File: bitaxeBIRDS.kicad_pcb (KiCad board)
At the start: 6 copper layers, 65 x 120 mm, 204 parts, among them J1 XT30, J4 Conn_01x04, U12 TLV75512PDQNR, U13 EMC2103-2, U14 TLV75512PDQNR, U15 TLV75512PDQNR, U2 TPS546D24ARVFR, U3 TLV75512PDQNR, U5 TPS22919DCKR, U8 SN74AVC4T774, U9 Raspberry Pi Pico, Y2 50MHz

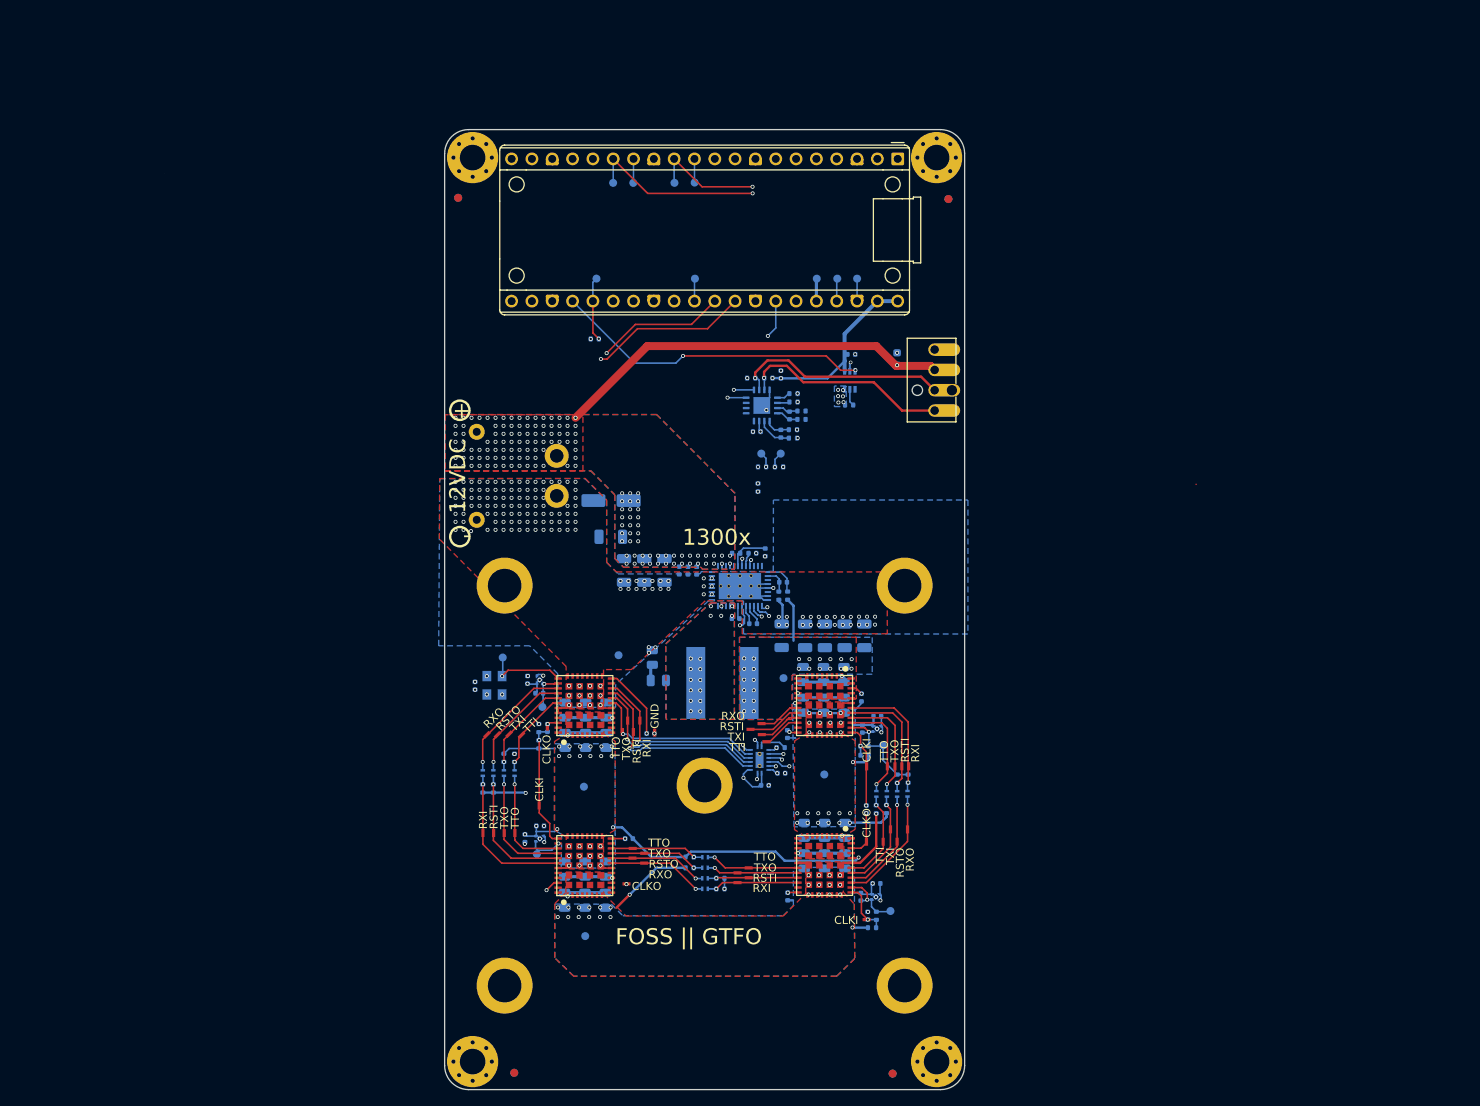
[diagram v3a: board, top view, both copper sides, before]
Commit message: Removed EMC2103, added discrete fan control, DRC pass, fixed logo.
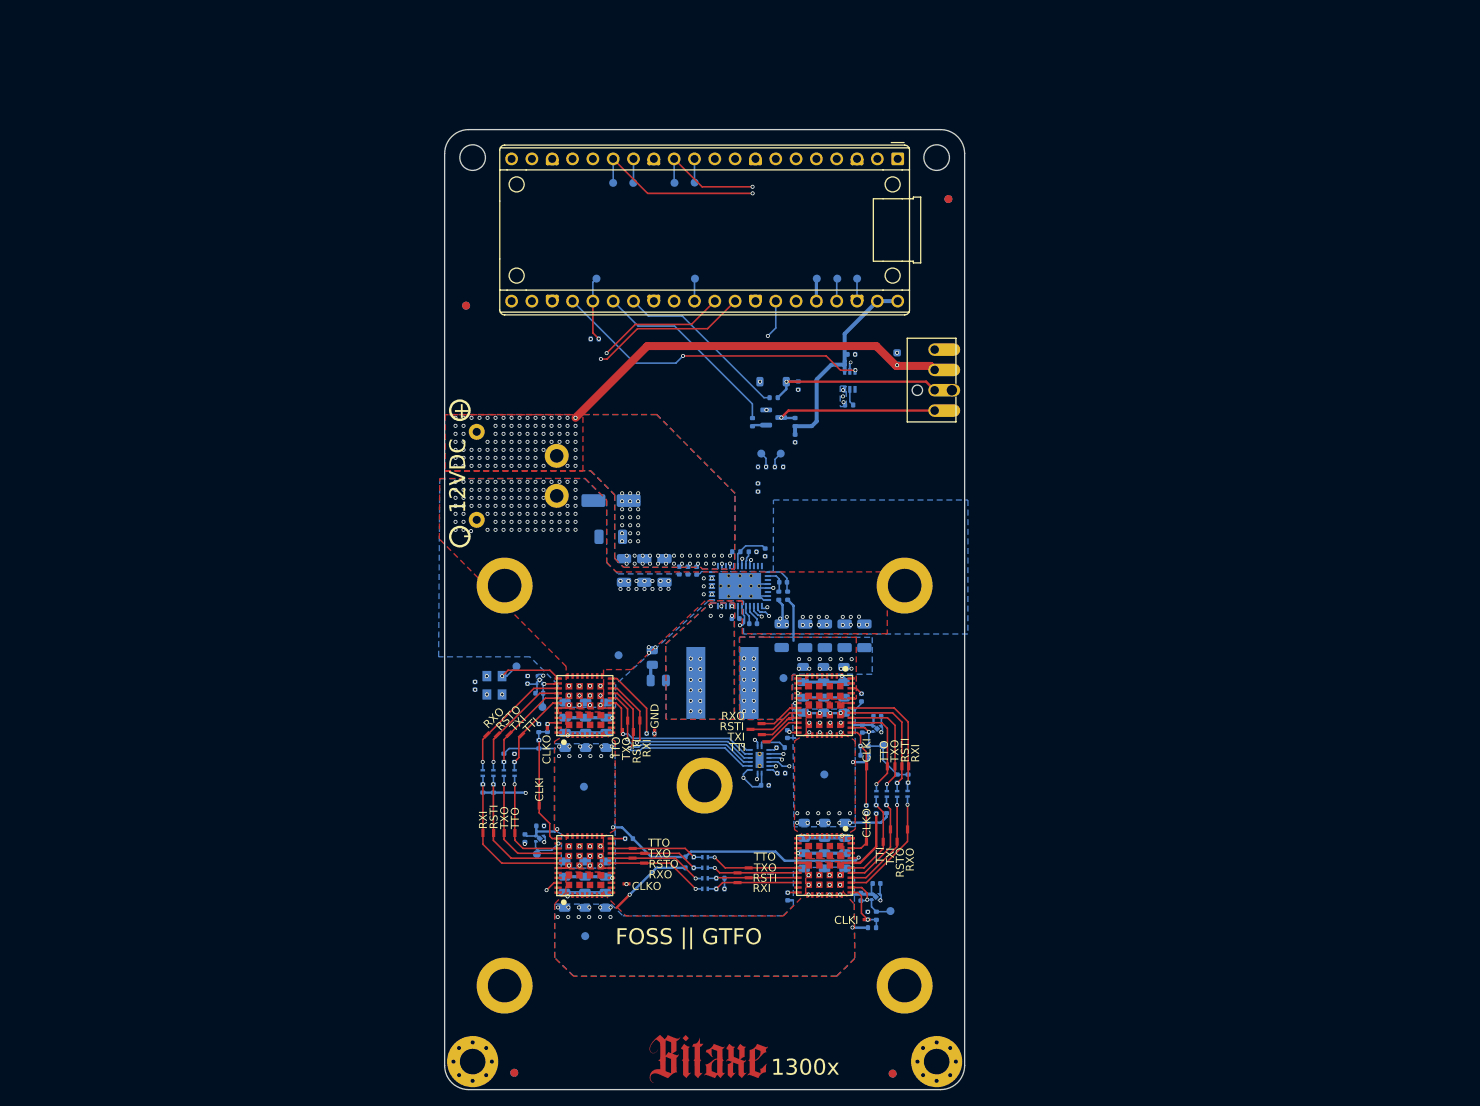
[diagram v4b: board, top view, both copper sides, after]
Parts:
- removed C73, C74: 470pF, Capacitor_SMD:C_0402_1005Metric
- removed C75: 0.1uF, Capacitor_SMD:C_0402_1005Metric
- removed the G*** at (76.8, 29.8)
- removed R27, R28, R29, R30: 0, Resistor_SMD:R_0402_1005Metric
- removed R31: 10k, Resistor_SMD:R_0402_1005Metric
- removed R32: Rtrip, Resistor_SMD:R_0402_1005Metric
- removed U13: EMC2103-2, Package_DFN_QFN:QFN-16-1EP_4x4mm_P0.65mm_EP2.1x2.1mm
- added D13: 3.3V Zener, Diode_SMD:D_SOD-123, B.Cu at (139.6, 61.5)
- added G***: LOGO, bitaxe:bitaxe_logo_small, F.Cu at (131.5, 146.2)
- added Q1: BSS138, Package_TO_SOT_SMD:SOT-23, B.Cu at (139.6, 66.0)
- added R1: 1k, Resistor_SMD:R_0402_1005Metric, B.Cu at (137.0, 66.6)
- added R2: 10k, Resistor_SMD:R_0402_1005Metric, B.Cu at (139.6, 63.5)
- H1, H2: footprint MountingHole:MountingHole_3.2mm_M3_Pad_Via -> MountingHole:MountingHole_3.2mm_M3
- TP1: value PWR_EN -> PWR EN
- TP5: value 3V3_EN -> 3V3 EN
- U5: footprint emberone:DCK0006A_N -> bitaxe:DCK0006A_N
- moved FID4 13.5 mm to (101.2, 52.0)
- moved C77 8.19 mm to (142.3, 68.6), turned to -90 degrees
- moved R34 6.43 mm to (142.3, 66.6), turned to -90 degrees
- moved R33 5.96 mm to (142.7, 62.0), turned to -90 degrees
- moved TP10 2.05 mm to (107.5, 97.1), turned to -90 degrees
- moved C11 0.19 mm to (137.0, 82.8)
- moved R5 0.19 mm to (135.0, 82.8)
- turned TP7 to -90 degrees
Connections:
- net /fan/FAN_PWM renamed /fan/FAN_PWM_PIN
- net /fan/FAN_TACH renamed /fan/FAN_TACH_PIN
- U9 pad 26: unconnected-(U9-GP20-Pad26) -> /Data/FAN_PWM
- U9 pad 27: unconnected-(U9-GP21-Pad27) -> /Data/FAN_TACH
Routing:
- net /Data/FAN_PWM: track 0.00 -> 24.5 mm
- net /Data/FAN_TACH: track 0.00 -> 22.0 mm
- net /3V3: track 110.3 -> 91.6 mm, vias 7 -> 5
- net /fan/FAN_PWM_PIN: track 26.2 -> 21.3 mm
- net Net-(U13-DP1): track 4.39 -> 0.00 mm
- net /fan/FAN_TACH_PIN: track 27.3 -> 22.9 mm
- net /5V: track 23.0 -> 26.5 mm, vias 2 -> 0
- net Net-(U13-DN1): track 3.16 -> 0.00 mm
- net Net-(U13-DP2): track 2.82 -> 0.00 mm
- net Net-(U13-DN2): track 2.72 -> 0.00 mm
- net GND: track 31.8 -> 29.2 mm, vias 177 -> 171
- net /Data/SCL: track 92.9 -> 90.4 mm, vias 3 -> 2
- net /Data/SDA: track 86.4 -> 84.0 mm, vias 3 -> 2
- net Net-(Q1-G): track 0.00 -> 1.77 mm
- net Net-(U13-SHDN_SEL): track 1.72 -> 0.00 mm
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
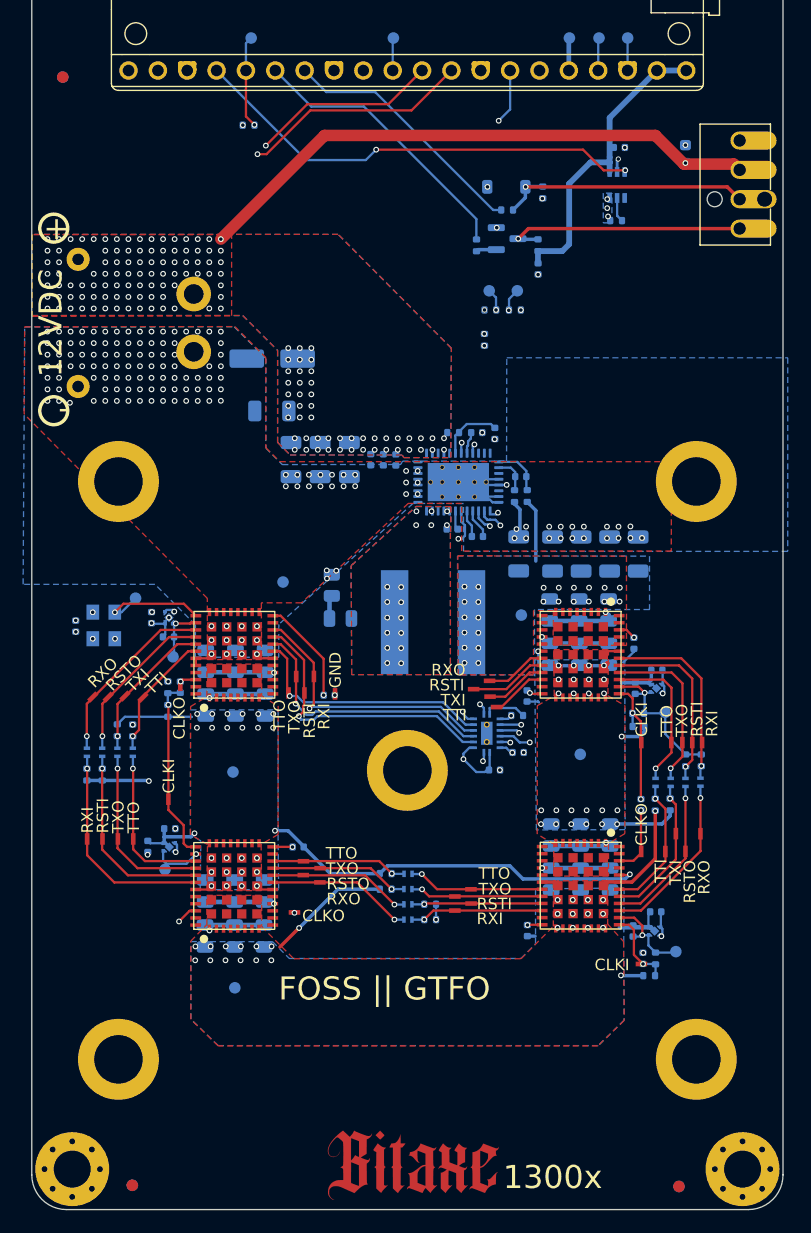
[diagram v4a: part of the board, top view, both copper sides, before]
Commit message: power plane cleanup. added field vias. generated BOM
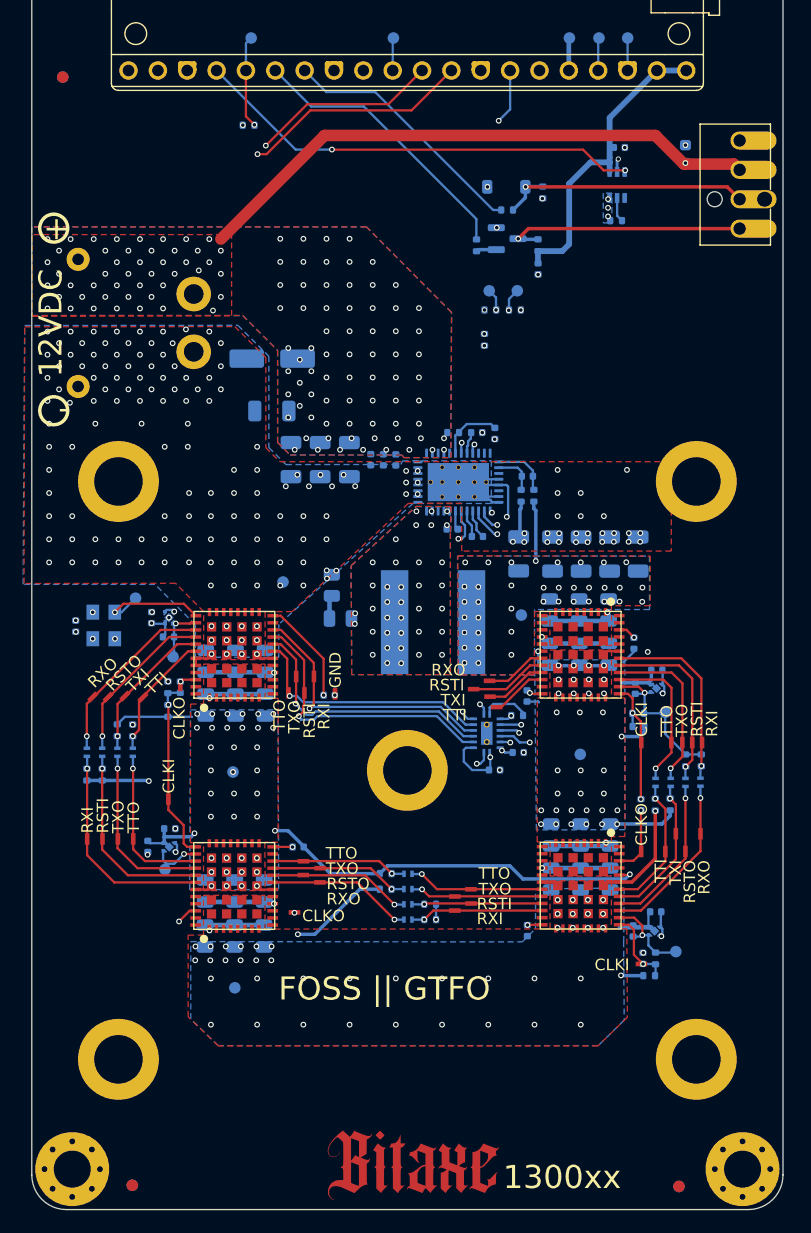
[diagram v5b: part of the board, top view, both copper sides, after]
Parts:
- moved C18 0.57 mm to (141.4, 86.5)
- moved R7 0.57 mm to (141.9, 88.2)
- moved R8 0.57 mm to (140.8, 88.2)
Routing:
- net /ASIC/GND4: track 80.1 -> 85.9 mm, vias 27 -> 36
- net /Power/AGND: track 7.66 -> 13.3 mm
- net /Data/SDA: track 84.0 -> 81.3 mm
- net /Data/SCL: track 90.4 -> 88.1 mm
- net /Power/PGOOD: track 58.6 -> 57.7 mm
- net /Data/5V_EN: track 39.7 -> 38.9 mm
- net /ASIC/1V2-3: track 32.1 -> 32.7 mm
- net Net-(U2-GOSNS): track 3.20 -> 3.75 mm
- net Net-(U2-VOSNS): track 4.40 -> 4.96 mm
- net /ASIC/1V2-2: track 26.9 -> 26.4 mm
- net GND: track 29.2 -> 29.7 mm, vias 171 -> 180
- net /3V3: track 91.6 -> 91.2 mm, vias 5 -> 6
- net /VDD: track 5.43 -> 5.22 mm, vias 24 -> 38
- net /ASIC/GND3: track 121.5 -> 121.7 mm, vias 28 -> 46
- net /Power/SW1: vias 18 -> 37
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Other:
- board text added: "1300xx"
- board text removed: "1300x"

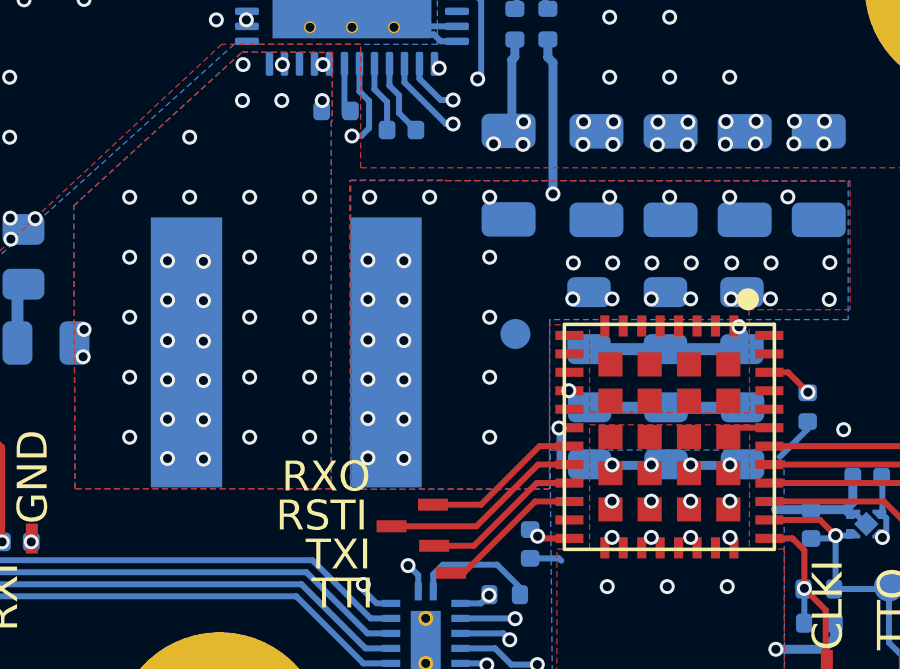
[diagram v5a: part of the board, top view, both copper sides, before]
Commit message: update TPS546D24 to `S` variant. Add render and readme.
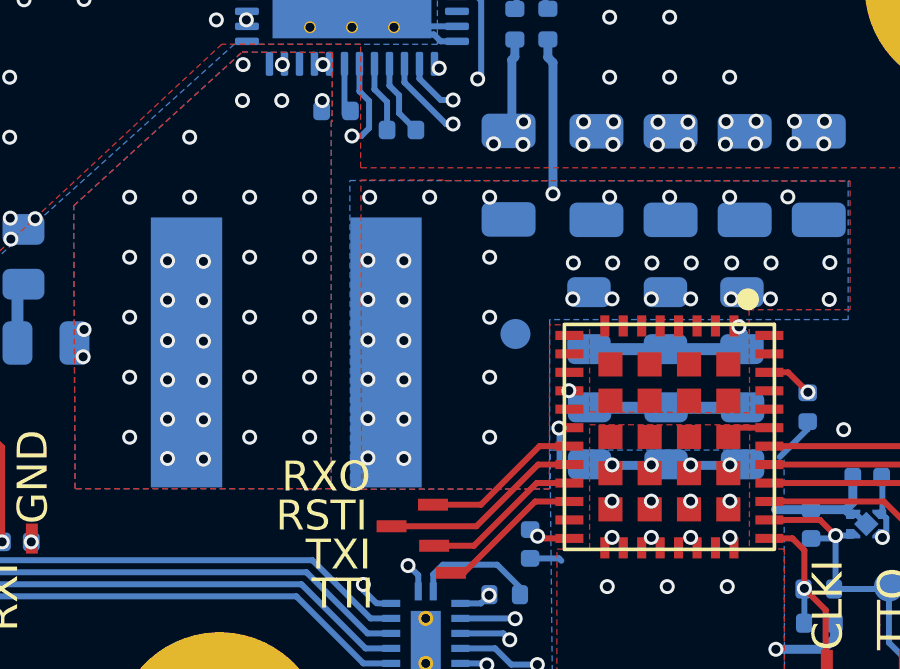
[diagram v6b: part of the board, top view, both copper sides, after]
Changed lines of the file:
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@@
 		(embedded_fonts no)
 		(model "${KIPRJMOD}/3d/GT heatsink.step"
-			(hide yes)
 			(offset
 				(xyz 0 -29 32.5)
@@
 		)
 		(model "${KIPRJMOD}/3d/Fan 60x60x25mm.stp"
-			(hide yes)
 			(offset
 				(xyz -5.5 41 33.5)
@@
 	)
 	(gr_rect
-		(start 112.71 85.17)
+		(start 112.71 85.295)
 		(end 149.57 88.92)
 		(stroke
@@
 				(xy 138.505539 93.427006) (xy 138.505632 93.446105) (xy 152.014955 93.457196) (xy 152.014955 97.75)
 				(xy 148.646389 97.75) (xy 148.66744 101.187985) (xy 143.330397 101.159097) (xy 143.33 98.25664)
-				(xy 141.997002 98.253492) (xy 141.987815 103.723186) (xy 135.392349 103.734687) (xy 135.368086 93.427069)
+				(xy 141.997002 98.253492) (xy 141.987815 103.723186) (xy 135.732254 103.734094) (xy 135.707992 93.427062)
 			)
 		)
